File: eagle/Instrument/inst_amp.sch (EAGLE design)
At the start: 12 parts, among them IC1 INA126U, X1 VCC +/-, X2 Vin, X3 Vout

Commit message: PCB design done
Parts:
- removed LED1: (no value), led:LEDCHIPLED_1206
- added C6, C7: 100nF, rcl:C-EU050-025X075
- added IC2: OP07C, burr-brown:OPA658P
- added R4: 360R, rcl:R-EU_0207/10
- C1, C2: device rcl:C-EUC1206 -> rcl:C-EU050-025X075
- C3, C4: value 0,47µF -> 100µF; device rcl:CPOL-EU153CLV-0405 -> rcl:CPOL-EUE5-10.5
- IC1: value INA126U -> INA126P; device burr-brown:INA126U -> burr-brown:INA126P
- R1: value 18k -> 8k; device resistor:R-EU_R1206 -> rcl:R-EU_0207/10
- R2: value 330R -> 180R; device resistor:R-EU_R1206 -> rcl:R-EU_0207/10
- R3: value 0R33 -> 0R2; device rcl:R-EU_VTA55 -> rcl:R-EU_0414/15
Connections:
- removed net N$3: C1.1, C4.+, IC1.V-, X1-2.S
- removed net N$8: LED1.A, R2.1
- new net N$4: IC2.+IN, R2.1, R4.2
- new net REF: IC1.REF, IC2.-IN, IC2.OUT
- new net V-: C2.1, C3.+, C6.1, IC1.V-, IC2.V-, R4.1, X1-2.S
- net GND: now also C6.2, C7.1; no longer LED1.C
- net V+: now also C1.1, C4.+, C7.2, IC2.V+; no longer C2.1, C3.+
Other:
- moved on the sheet: C1, C2, C3, C4, IC1, R1, R2, R3, X1-1, X1-2, X2-1, X2-2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

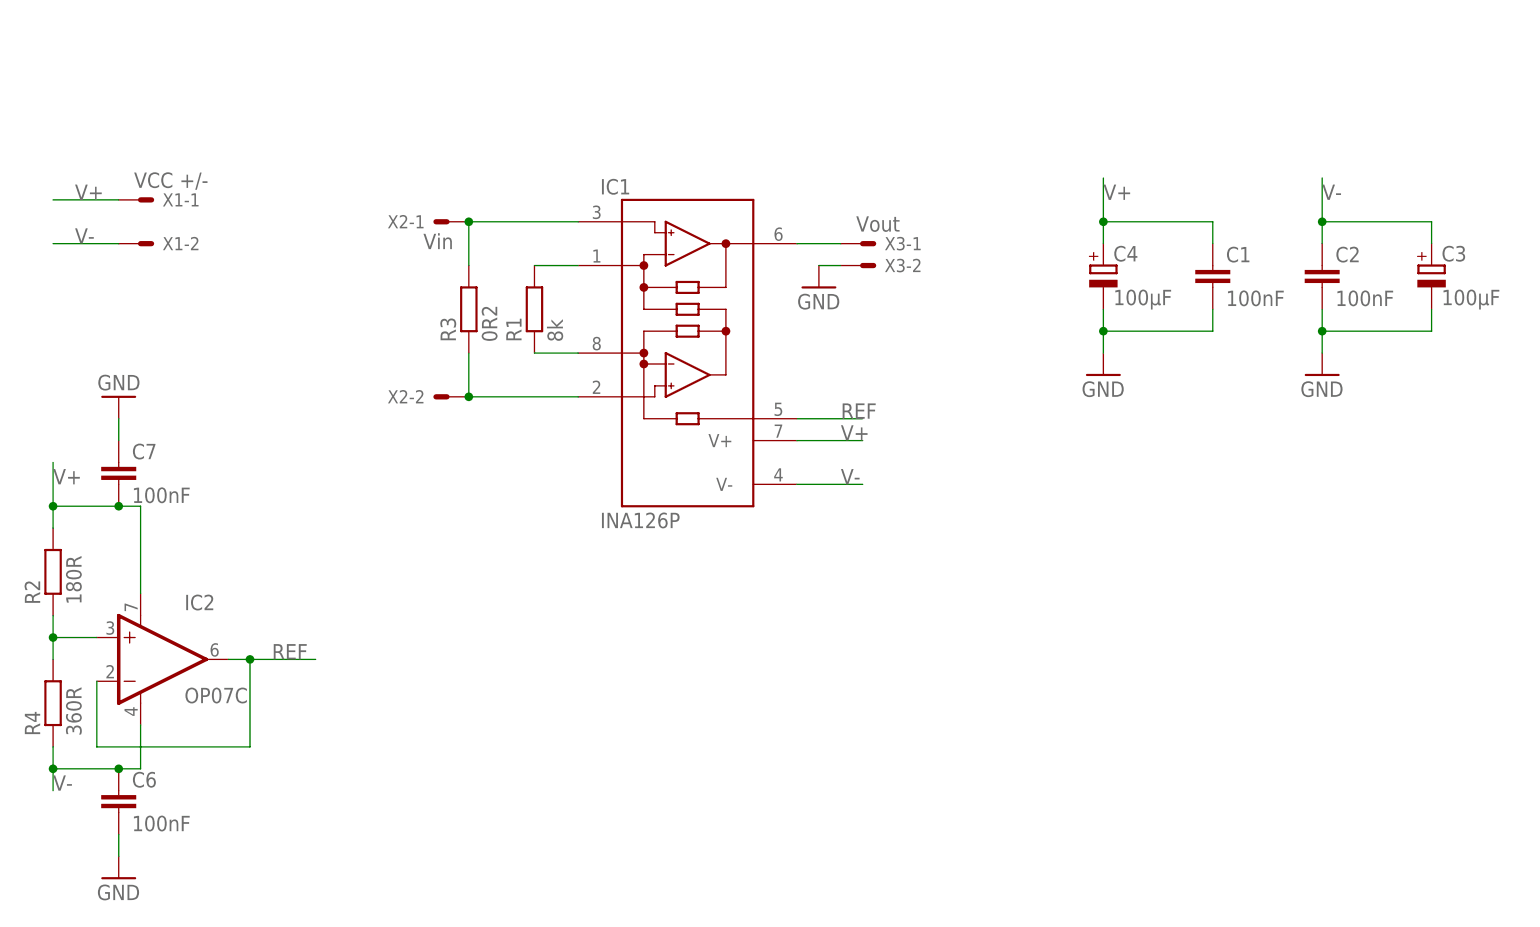
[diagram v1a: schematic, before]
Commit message: Added lo pass filter
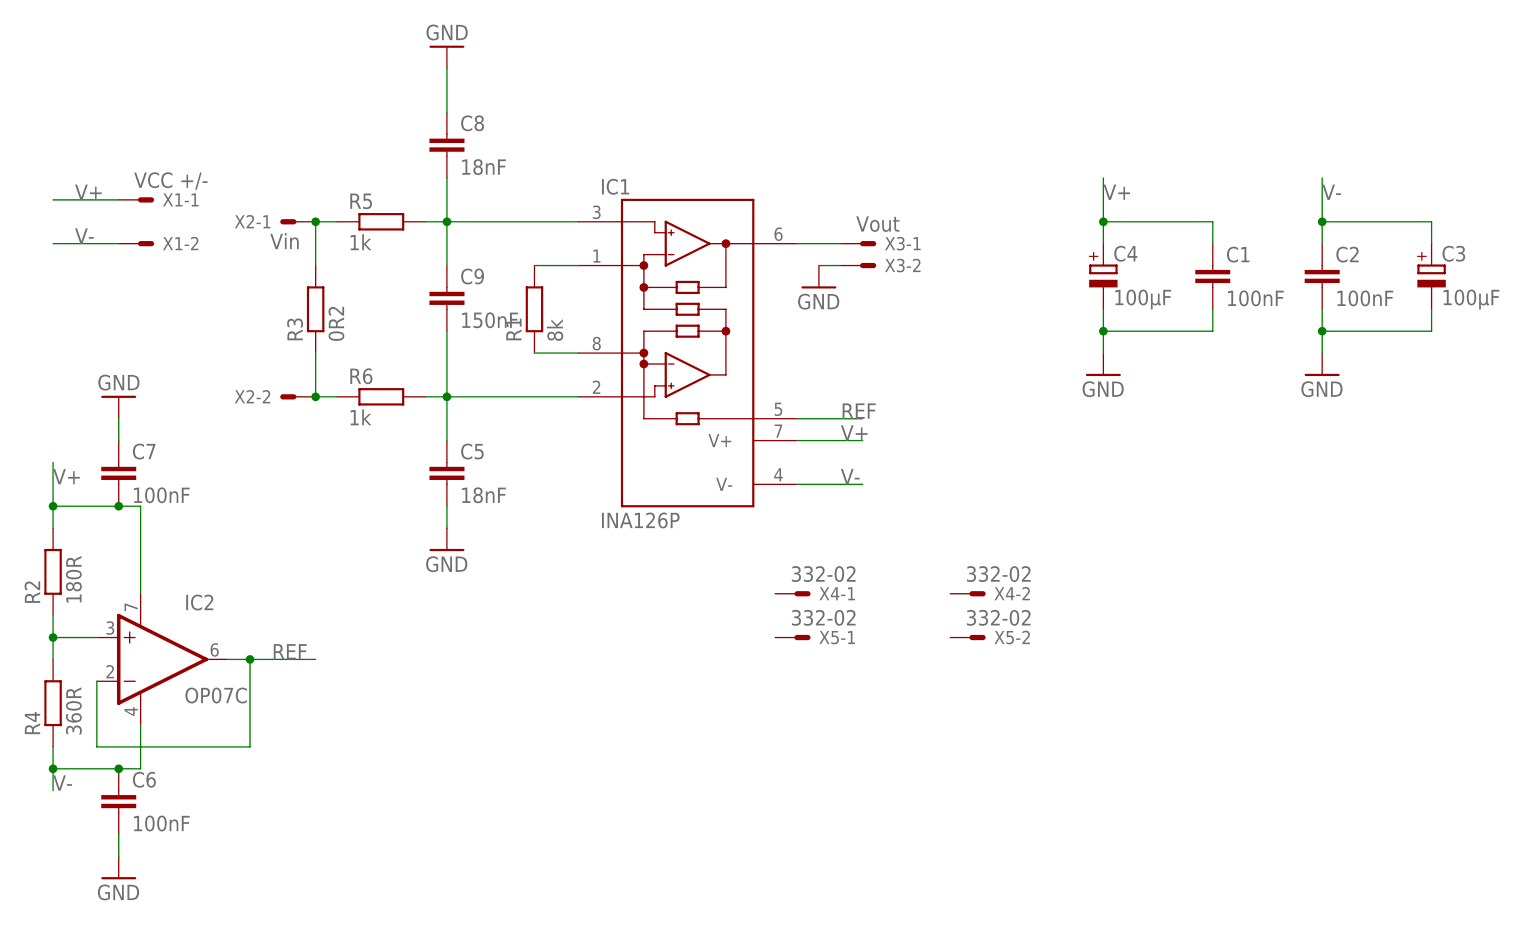
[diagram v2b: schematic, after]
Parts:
- added C5, C8: 18nF, rcl:C-EU050-024X044
- added C9: 150nF, rcl:C-EU050-025X075
- added R5, R6: 1k, resistor:R-EU_0207/10
- added X4, X5: 332-02, con-garry:332-02
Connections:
- new net N$3: R3.1, R6.1, X2-2.S
- new net N$8: R3.2, R5.1, X2-1.S
- net GND: now also C5.2, C8.1
- net N$6: now also C8.2, C9.1, R5.2; no longer R3.2, X2-1.S
- net N$7: now also C5.1, C9.2, R6.2; no longer R3.1, X2-2.S
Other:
- moved on the sheet: R3, X2-1, X2-2
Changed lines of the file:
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@@
 <grid distance="0.1" unitdist="inch" unit="inch" style="lines" multiple="1" display="no" altdistance="0.01" altunitdist="inch" altunit="inch"/>
 <layers>
-<layer number="1" name="Top" color="4" fill="1" visible="yes" active="no"/>
-<layer number="16" name="Bottom" color="1" fill="1" visible="yes" active="no"/>
-<layer number="17" name="Pads" color="2" fill="1" visible="yes" active="no"/>
-<layer number="18" name="Vias" color="2" fill="1" visible="yes" active="no"/>
-<layer number="19" name="Unrouted" color="6" fill="1" visible="yes" active="no"/>
-<layer number="20" name="Dimension" color="15" fill="1" visible="yes" active="no"/>
-<layer number="21" name="tPlace" color="7" fill="1" visible="yes" active="no"/>
-<layer number="22" name="bPlace" color="7" fill="1" visible="yes" active="no"/>
-<layer number="23" name="tOrigins" color="15" fill="1" visible="yes" active="no"/>
-<layer number="24" name="bOrigins" color="15" fill="1" visible="yes" active="no"/>
-<layer number="25" name="tNames" color="7" fill="1" visible="yes" active="no"/>
-<layer number="26" name="bNames" color="7" fill="1" visible="yes" active="no"/>
-<layer number="27" name="tValues" color="7" fill="1" visible="yes" active="no"/>
-<layer number="28" name="bValues" color="7" fill="1" visible="yes" active="no"/>
+<layer number="1" name="Top" color="4" fill="1" visible="no" active="no"/>
+<layer number="16" name="Bottom" color="1" fill="1" visible="no" active="no"/>
+<layer number="17" name="Pads" color="2" fill="1" visible="no" active="no"/>
+<layer number="18" name="Vias" color="2" fill="1" visible="no" active="no"/>
+<layer number="19" name="Unrouted" color="6" fill="1" visible="no" active="no"/>
+<layer number="20" name="Dimension" color="15" fill="1" visible="no" active="no"/>
+<layer number="21" name="tPlace" color="7" fill="1" visible="no" active="no"/>
+<layer number="22" name="bPlace" color="7" fill="1" visible="no" active="no"/>
+<layer number="23" name="tOrigins" color="15" fill="1" visible="no" active="no"/>
+<layer number="24" name="bOrigins" color="15" fill="1" visible="no" active="no"/>
+<layer number="25" name="tNames" color="7" fill="1" visible="no" active="no"/>
+<layer number="26" name="bNames" color="7" fill="1" visible="no" active="no"/>
+<layer number="27" name="tValues" color="7" fill="1" visible="no" active="no"/>
+<layer number="28" name="bValues" color="7" fill="1" visible="no" active="no"/>
 <layer number="29" name="tStop" color="7" fill="3" visible="no" active="no"/>
 <layer number="30" name="bStop" color="7" fill="6" visible="no" active="no"/>
@@
 <layer number="35" name="tGlue" color="7" fill="4" visible="no" active="no"/>
 <layer number="36" name="bGlue" color="7" fill="5" visible="no" active="no"/>
-<layer number="37" name="tTest" color="7" fill="1" visible="yes" active="no"/>
-<layer number="38" name="bTest" color="7" fill="1" visible="yes" active="no"/>
+<layer number="37" name="tTest" color="7" fill="1" visible="no" active="no"/>
+<layer number="38" name="bTest" color="7" fill="1" visible="no" active="no"/>
 <layer number="39" name="tKeepout" color="4" fill="11" visible="no" active="no"/>
 <layer number="40" name="bKeepout" color="1" fill="11" visible="no" active="no"/>
@@
 <layer number="44" name="Drills" color="7" fill="1" visible="no" active="no"/>
 <layer number="45" name="Holes" color="7" fill="1" visible="no" active="no"/>
-<layer number="46" name="Milling" color="3" fill="1" visible="yes" active="no"/>
-<layer number="47" name="Measures" color="7" fill="1" visible="yes" active="no"/>
-<layer number="48" name="Document" color="7" fill="1" visible="yes" active="no"/>
-<layer number="49" name="Reference" color="7" fill="1" visible="yes" active="no"/>
-<layer number="51" name="tDocu" color="7" fill="1" visible="yes" active="no"/>
-<layer number="52" name="bDocu" color="7" fill="1" visible="yes" active="no"/>
+<layer number="46" name="Milling" color="3" fill="1" visible="no" active="no"/>
+<layer number="47" name="Measures" color="7" fill="1" visible="no" active="no"/>
+<layer number="48" name="Document" color="7" fill="1" visible="no" active="no"/>
+<layer number="49" name="Reference" color="7" fill="1" visible="no" active="no"/>
+<layer number="51" name="tDocu" color="7" fill="1" visible="no" active="no"/>
+<layer number="52" name="bDocu" color="7" fill="1" visible="no" active="no"/>
 <layer number="91" name="Nets" color="2" fill="1" visible="yes" active="yes"/>
 <layer number="92" name="Busses" color="1" fill="1" visible="yes" active="yes"/>
@@
 <part name="GND4" library="supply1" deviceset="GND" device=""/>
 <part name="GND5" library="supply1" deviceset="GND" device=""/>
+<part name="C5" library="rcl" deviceset="C-EU" device="050-024X044" value="18nF"/>
+<part name="C8" library="rcl" deviceset="C-EU" device="050-024X044" value="18nF"/>
+<part name="C9" library="rcl" deviceset="C-EU" device="050-025X075" value="150nF"/>
+<part name="GND6" library="supply1" deviceset="GND" device=""/>
+<part name="GND7" library="supply1" deviceset="GND" device=""/>
+<part name="R5" library="resistor" deviceset="R-EU_" device="0207/10" value="1k"/>
+<part name="R6" library="resistor" deviceset="R-EU_" device="0207/10" value="1k"/>
+<part name="X4" library="con-garry" deviceset="332-02" device=""/>
+<part name="X5" library="con-garry" deviceset="332-02" device=""/>
 </parts>
 <sheets>
@@
 <instance part="X1" gate="-1" x="2.54" y="91.44"/>
 <instance part="X1" gate="-2" x="2.54" y="86.36"/>
-<instance part="X2" gate="-1" x="38.1" y="88.9" rot="R180"/>
-<instance part="X2" gate="-2" x="38.1" y="68.58" rot="R180"/>
+<instance part="X2" gate="-1" x="20.32" y="88.9" rot="R180"/>
+<instance part="X2" gate="-2" x="20.32" y="68.58" rot="R180"/>
 <instance part="X3" gate="-1" x="86.36" y="86.36"/>
 <instance part="X3" gate="-2" x="86.36" y="83.82"/>
 <instance part="C3" gate="G$1" x="152.4" y="83.82"/>
 <instance part="C4" gate="G$1" x="114.3" y="83.82"/>
-<instance part="R3" gate="G$1" x="40.64" y="78.74" rot="R90"/>
+<instance part="R3" gate="G$1" x="22.86" y="78.74" rot="R90"/>
 <instance part="GND2" gate="1" x="81.28" y="81.28"/>
 <instance part="GND3" gate="1" x="114.3" y="71.12"/>
@@
 <instance part="GND4" gate="1" x="0" y="68.58" rot="R180"/>
 <instance part="GND5" gate="1" x="0" y="12.7"/>
+<instance part="C5" gate="G$1" x="38.1" y="60.96"/>
+<instance part="C8" gate="G$1" x="38.1" y="99.06"/>
+<instance part="C9" gate="G$1" x="38.1" y="81.28"/>
+<instance part="GND6" gate="1" x="38.1" y="109.22" rot="R180"/>
+<instance part="GND7" gate="1" x="38.1" y="50.8"/>
+<instance part="R5" gate="G$1" x="30.48" y="88.9"/>
+<instance part="R6" gate="G$1" x="30.48" y="68.58"/>
+<instance part="X4" gate="-1" x="78.74" y="45.72"/>
+<instance part="X4" gate="-2" x="99.06" y="45.72"/>
+<instance part="X5" gate="-1" x="78.74" y="40.64"/>
+<instance part="X5" gate="-2" x="99.06" y="40.64"/>
 </instances>
 <busses>
@@
 <wire x1="0" y1="17.78" x2="0" y2="15.24" width="0.1524" layer="91"/>
 <pinref part="GND5" gate="1" pin="GND"/>
+</segment>
+<segment>
+<pinref part="C8" gate="G$1" pin="1"/>
+<wire x1="38.1" y1="101.6" x2="38.1" y2="106.68" width="0.1524" layer="91"/>
+<pinref part="GND6" gate="1" pin="GND"/>
+</segment>
+<segment>
+<pinref part="C5" gate="G$1" pin="2"/>
+<wire x1="38.1" y1="55.88" x2="38.1" y2="53.34" width="0.1524" layer="91"/>
+<pinref part="GND7" gate="1" pin="GND"/>
 </segment>
 </net>
@@
 <net name="N$6" class="0">
 <segment>
-<pinref part="X2" gate="-1" pin="S"/>
 <pinref part="IC1" gate="G$1" pin="+IN"/>
-<wire x1="40.64" y1="88.9" x2="53.34" y2="88.9" width="0.1524" layer="91"/>
-<pinref part="R3" gate="G$1" pin="2"/>
-<wire x1="40.64" y1="88.9" x2="40.64" y2="83.82" width="0.1524" layer="91"/>
-<junction x="40.64" y="88.9"/>
+<wire x1="35.56" y1="88.9" x2="38.1" y2="88.9" width="0.1524" layer="91"/>
+<wire x1="38.1" y1="88.9" x2="53.34" y2="88.9" width="0.1524" layer="91"/>
+<pinref part="C9" gate="G$1" pin="1"/>
+<wire x1="38.1" y1="83.82" x2="38.1" y2="88.9" width="0.1524" layer="91"/>
+<junction x="38.1" y="88.9"/>
+<pinref part="C8" gate="G$1" pin="2"/>
+<wire x1="38.1" y1="93.98" x2="38.1" y2="88.9" width="0.1524" layer="91"/>
+<pinref part="R5" gate="G$1" pin="2"/>
 </segment>
 </net>
@@
 <segment>
 <pinref part="IC1" gate="G$1" pin="-IN"/>
-<pinref part="X2" gate="-2" pin="S"/>
-<wire x1="53.34" y1="68.58" x2="40.64" y2="68.58" width="0.1524" layer="91"/>
-<pinref part="R3" gate="G$1" pin="1"/>
-<wire x1="40.64" y1="73.66" x2="40.64" y2="68.58" width="0.1524" layer="91"/>
-<junction x="40.64" y="68.58"/>
+<wire x1="53.34" y1="68.58" x2="38.1" y2="68.58" width="0.1524" layer="91"/>
+<wire x1="38.1" y1="68.58" x2="35.56" y2="68.58" width="0.1524" layer="91"/>
+<pinref part="C5" gate="G$1" pin="1"/>
+<wire x1="38.1" y1="63.5" x2="38.1" y2="68.58" width="0.1524" layer="91"/>
+<junction x="38.1" y="68.58"/>
+<pinref part="C9" gate="G$1" pin="2"/>
+<wire x1="38.1" y1="68.58" x2="38.1" y2="76.2" width="0.1524" layer="91"/>
+<pinref part="R6" gate="G$1" pin="2"/>
 </segment>
 </net>
@@
 </segment>
 </net>
+<net name="N$3" class="0">
+<segment>
+<pinref part="X2" gate="-2" pin="S"/>
+<pinref part="R6" gate="G$1" pin="1"/>
+<wire x1="25.4" y1="68.58" x2="22.86" y2="68.58" width="0.1524" layer="91"/>
+<pinref part="R3" gate="G$1" pin="1"/>
+<wire x1="22.86" y1="73.66" x2="22.86" y2="68.58" width="0.1524" layer="91"/>
+<junction x="22.86" y="68.58"/>
+</segment>
+</net>
+<net name="N$8" class="0">
+<segment>
+<pinref part="R3" gate="G$1" pin="2"/>
+<pinref part="R5" gate="G$1" pin="1"/>
+<pinref part="X2" gate="-1" pin="S"/>
+<wire x1="22.86" y1="88.9" x2="25.4" y2="88.9" width="0.1524" layer="91"/>
+<junction x="22.86" y="88.9"/>
+<wire x1="22.86" y1="88.9" x2="22.86" y2="83.82" width="0.1524" layer="91"/>
+</segment>
+</net>

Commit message: Labb4 done
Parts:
- R2: value 180R -> 900R
- R4: value 360R -> 1100R
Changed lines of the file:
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@@
 <part name="GND1" library="supply1" deviceset="GND" device=""/>
 <part name="IC2" library="burr-brown" deviceset="OPA658" device="P" value="OP07C"/>
-<part name="R2" library="rcl" deviceset="R-EU_" device="0207/10" value="180R"/>
-<part name="R4" library="rcl" deviceset="R-EU_" device="0207/10" value="360R"/>
+<part name="R2" library="rcl" deviceset="R-EU_" device="0207/10" value="900R"/>
+<part name="R4" library="rcl" deviceset="R-EU_" device="0207/10" value="1100R"/>
 <part name="C6" library="rcl" deviceset="C-EU" device="050-025X075" value="100nF"/>
 <part name="C7" library="rcl" deviceset="C-EU" device="050-025X075" value="100nF"/>
